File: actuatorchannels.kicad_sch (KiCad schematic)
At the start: 3 parts

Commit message: Array of SSRs for actuation channels
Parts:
- added D? (x16): B2100A-13-F, Diode_SMD:D_SMA, symbol Device:D_Schottky_Small_Filled
- added J? (x16): ACT CH1, TerminalBlock_Phoenix:TerminalBlock_Phoenix_PT-1,5-2-5.0-H_1x02_P5.00mm_Horizontal, symbol Connector:Screw_Terminal_01x02
- added R? (x15): 270R, Resistor_SMD:R_0603_1608Metric, symbol Device:R_Small_US
- added U? (x15): TLP241A, actuation:11-5B2S, symbol actuation:TLP241A
- R?: value R_Small_US -> 270R; footprint (none) -> Resistor_SMD:R_0603_1608Metric; MPN (none) -> RC0603FR-07270RL
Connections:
- net ACT_CH1: now also R?.1, R?.1, R?.1, R?.1, R?.1, R?.1, R?.1, R?.1, R?.1, R?.1, R?.1, R?.1, R?.1, R?.1, R?.1
- net GND: now also U?.2, U?.2, U?.2, U?.2, U?.2, U?.2, U?.2, U?.2, U?.2, U?.2, U?.2, U?.2, U?.2, U?.2, U?.2
- net at U?.3: now also D?.1 (K), J?.1 (Pin_1)
- net Vdrive: now reaches U?.4
- net Vdrive: now also U?.4, U?.4, U?.4, U?.4, U?.4, U?.4, U?.4, U?.4, U?.4, U?.4, U?.4, U?.4, U?.4, U?.4, U?.4
- new net: R?.2, U?.1 (x15)
- new net: D?.1 (K), J?.1 (Pin_1), U?.3 (x15)
- new net GNDPWR: D?.2 (A), D?.2 (A), D?.2 (A), D?.2 (A), D?.2 (A), D?.2 (A), D?.2 (A), D?.2 (A), D?.2 (A), D?.2 (A), D?.2 (A), D?.2 (A), D?.2 (A), D?.2 (A), D?.2 (A), D?.2 (A), J?.2 (Pin_2), J?.2 (Pin_2), J?.2 (Pin_2), J?.2 (Pin_2), J?.2 (Pin_2), J?.2 (Pin_2), J?.2 (Pin_2), J?.2 (Pin_2), J?.2 (Pin_2), J?.2 (Pin_2), J?.2 (Pin_2), J?.2 (Pin_2), J?.2 (Pin_2), J?.2 (Pin_2), J?.2 (Pin_2), J?.2 (Pin_2)
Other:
- moved on the sheet: R?, U?
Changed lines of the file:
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@@
 (kicad_sch (version 20211123) (generator eeschema)
-  (paper "A3")
+  (paper "A2")

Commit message: Actuator channels complete
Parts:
- added C? (x2): 1uF, Capacitor_SMD:C_0603_1608Metric, symbol Device:C_Small
- added C? (x2): 0.1uF, Capacitor_SMD:C_0603_1608Metric, symbol Device:C_Small
- added U?: PCA9534, Package_SO:TSSOP-16_4.4x5mm_P0.65mm, symbol actuation:PCA9534
- J?: value ACT CH1 -> ACT CH3
- J?: value ACT CH1 -> ACT CH14
- J?: value ACT CH1 -> ACT CH2
- J?: value ACT CH1 -> ACT CH8
- J?: value ACT CH1 -> ACT CH12
- J?: value ACT CH1 -> ACT CH13
- J?: value ACT CH1 -> ACT CH7
- J?: value ACT CH1 -> ACT CH11
- J?: value ACT CH1 -> ACT CH16
- J?: value ACT CH1 -> ACT CH4
- J?: value ACT CH1 -> ACT CH9
- J?: value ACT CH1 -> ACT CH10
- J?: value ACT CH1 -> ACT CH15
- J?: value ACT CH1 -> ACT CH6
- J?: value ACT CH1 -> ACT CH5
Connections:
- net ACT_CH1: now also U?.4 (P0); no longer R?.1, R?.1, R?.1, R?.1, R?.1, R?.1, R?.1, R?.1, R?.1, R?.1, R?.1, R?.1, R?.1, R?.1, R?.1
- net GND: now also U?.1 (A0), U?.2 (A1), U?.3 (A2), U?.8 (GND), C?.2, C?.2, C?.2, C?.2, U?.2 (A1), U?.3 (A2), U?.8 (GND)
- net ACT_CH6: now reaches U?.10 (P5)
- net ACT_CH6: now also R?.1
- net ACT_CH7: now reaches U?.11 (P6)
- net ACT_CH7: now also R?.1
- net ACT_CH8: now reaches U?.12 (P7)
- net ACT_CH8: now also R?.1
- net SCL: now reaches U?.14 (SCL)
- net SCL: now also U?.14 (SCL)
- net SDA: now reaches U?.15 (SDA)
- net SDA: now also U?.15 (SDA)
- net +3.3V: now reaches U?.16 (VCC)
- net +3.3V: now also C?.1, C?.1, C?.1, C?.1, U?.1 (A0), U?.16 (VCC)
- net ACT_CH2: now reaches U?.5 (P1)
- net ACT_CH2: now also R?.1
- net ACT_CH3: now reaches U?.6 (P2)
- net ACT_CH3: now also R?.1
- net ACT_CH4: now reaches U?.7 (P3)
- net ACT_CH4: now also R?.1
- net ACT_CH5: now reaches U?.9 (P4)
- net ACT_CH5: now also R?.1
- new net ACT_CH10: R?.1, U?.5 (P1)
- new net ACT_CH11: R?.1, U?.6 (P2)
- new net ACT_CH12: R?.1, U?.7 (P3)
- new net ACT_CH13: R?.1, U?.9 (P4)
- new net ACT_CH14: R?.1, U?.10 (P5)
- new net ACT_CH15: R?.1, U?.11 (P6)
- new net ACT_CH16: R?.1, U?.12 (P7)
- new net ACT_CH9: R?.1, U?.4 (P0)
- no-connect marks 0 -> 2
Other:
- moved on the sheet: D?, J?, R?, U?
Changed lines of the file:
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@@
 (kicad_sch (version 20211123) (generator eeschema)
-  (paper "A2")
+  (paper "User" 299.999 350.012)

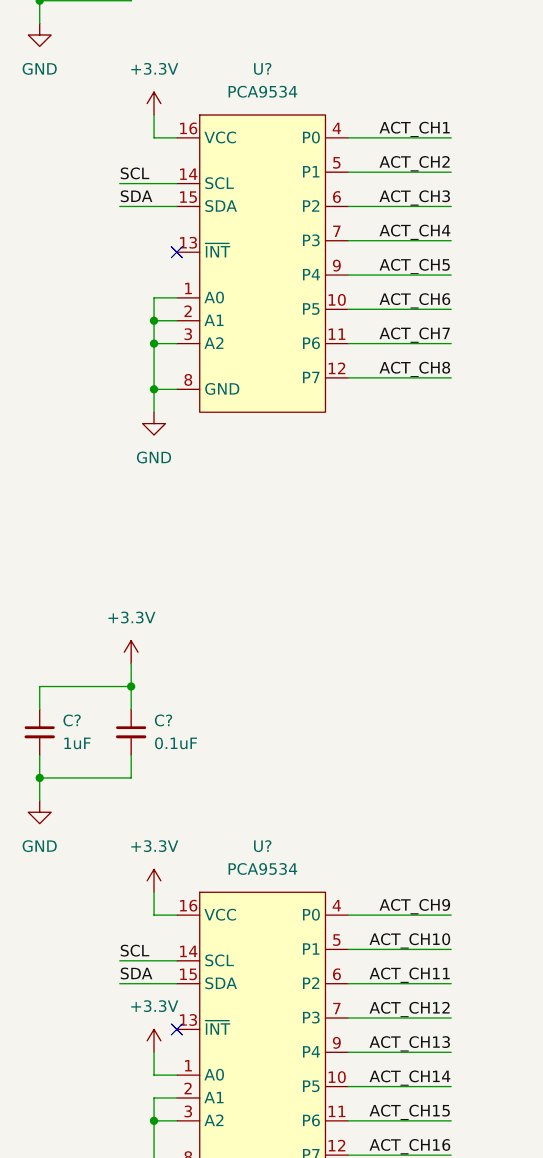
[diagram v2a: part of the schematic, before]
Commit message: Array of isolators for feedback channels
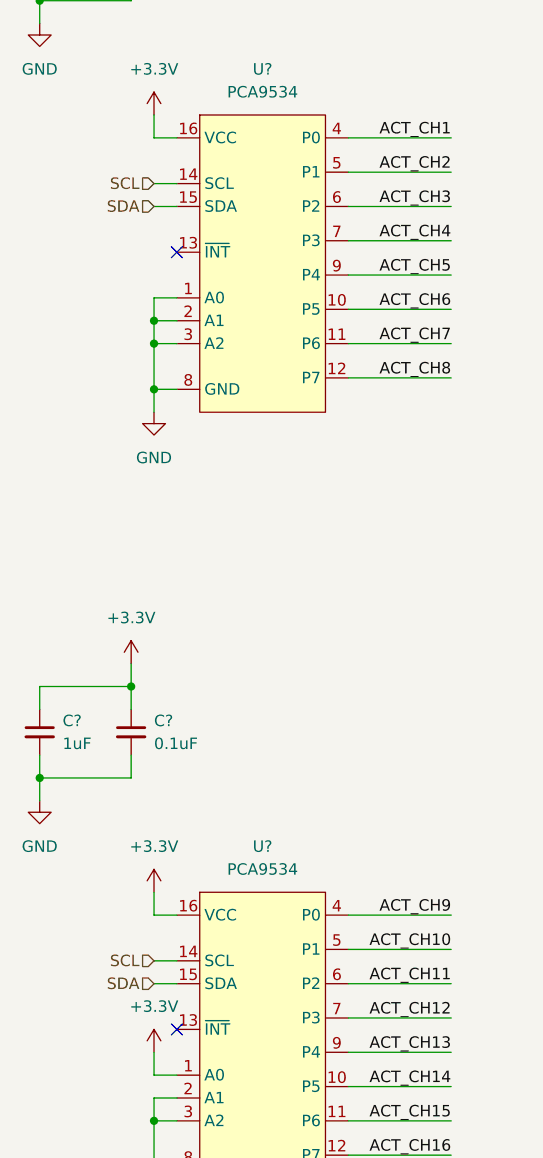
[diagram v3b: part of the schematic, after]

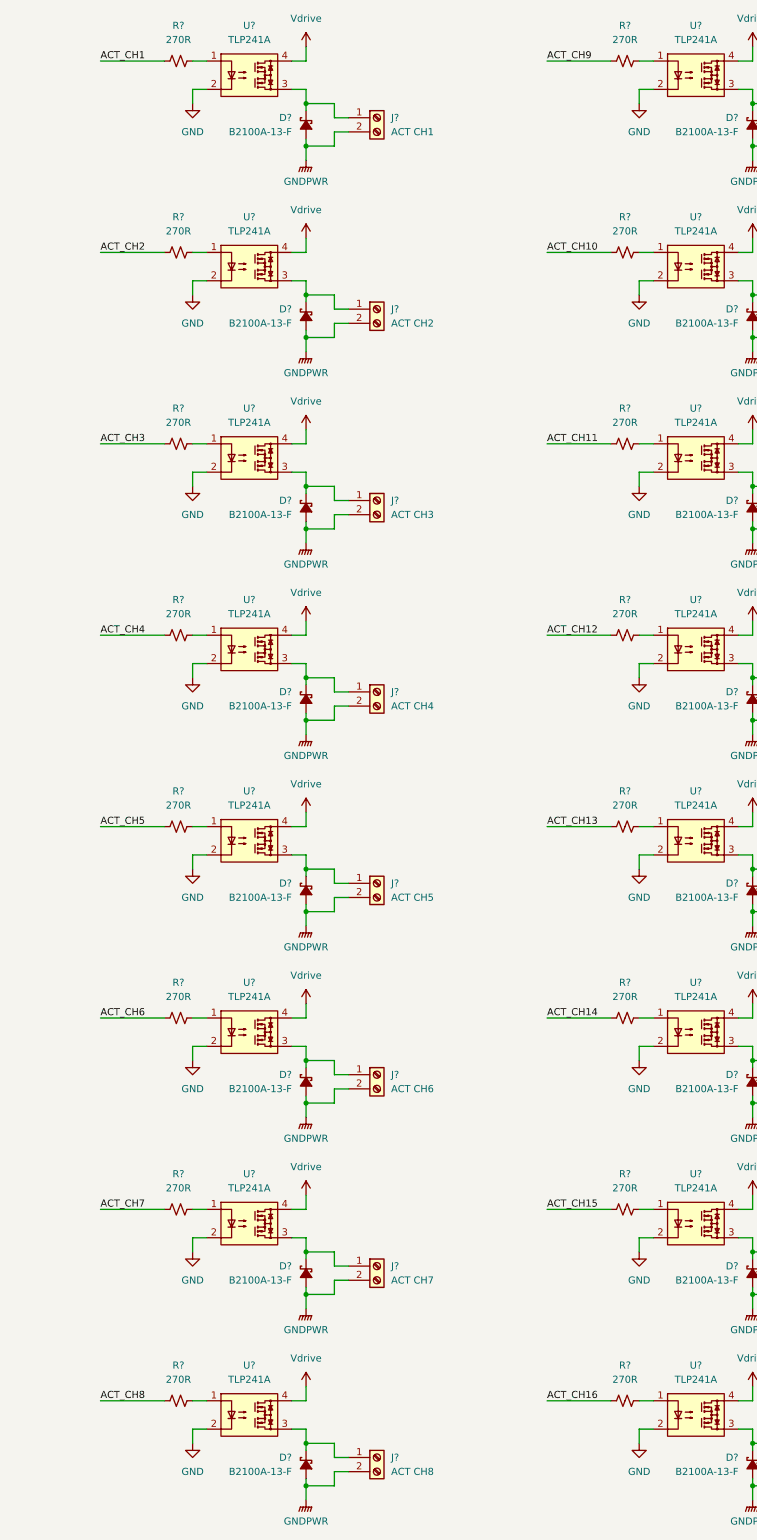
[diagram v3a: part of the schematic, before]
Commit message: Fixed actuator channels to make GPIO expander sink instead of source current
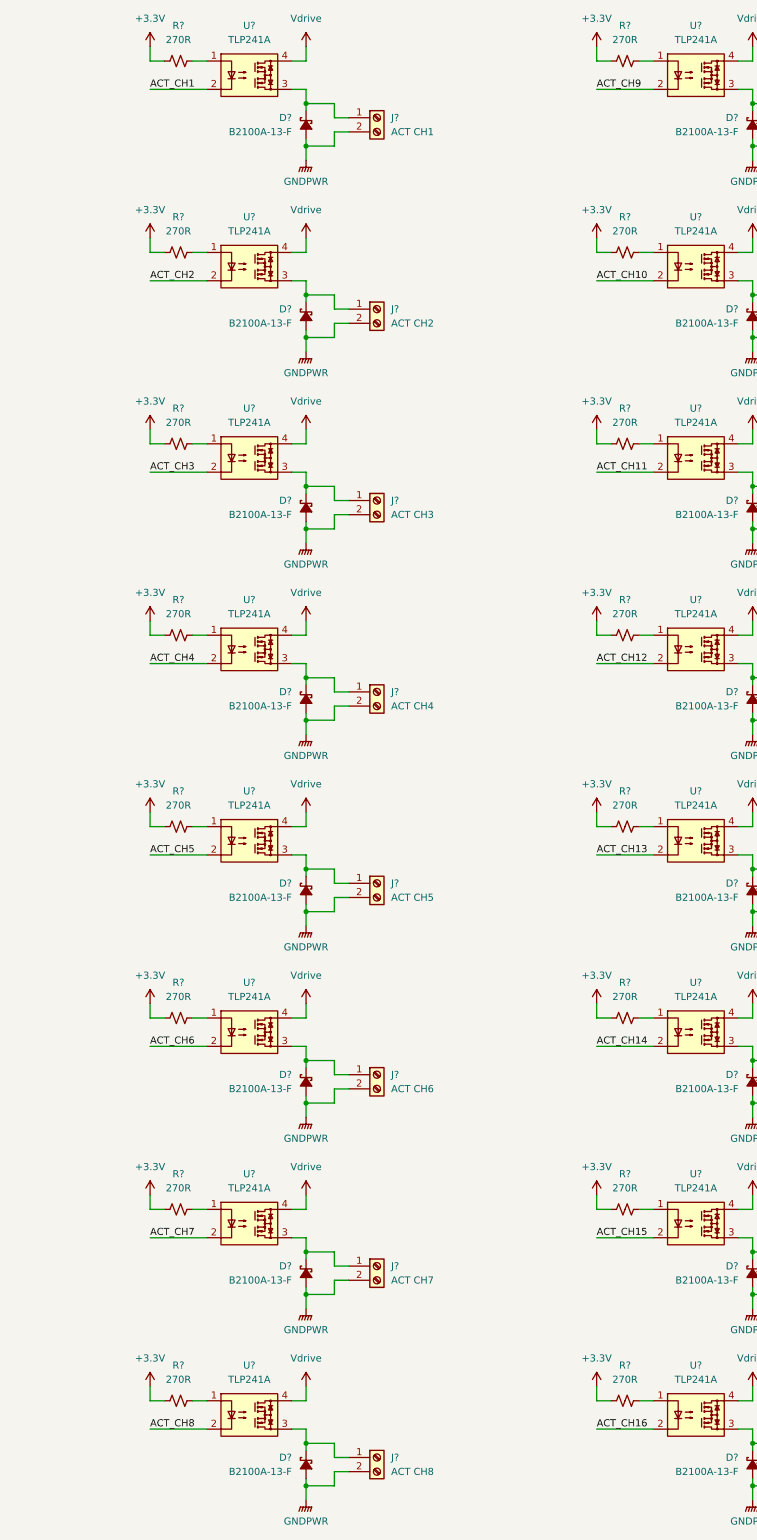
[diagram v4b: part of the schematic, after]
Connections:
- net +3.3V: now also R?.1, R?.1, R?.1, R?.1, R?.1, R?.1, R?.1, R?.1, R?.1, R?.1, R?.1, R?.1, R?.1, R?.1, R?.1, R?.1
- net ACT_CH1: now also U?.2; no longer R?.1
- net ACT_CH10: now also U?.2; no longer R?.1
- net ACT_CH11: now also U?.2; no longer R?.1
- net ACT_CH12: now also U?.2; no longer R?.1
- net ACT_CH13: now also U?.2; no longer R?.1
- net ACT_CH14: now also U?.2; no longer R?.1
- net ACT_CH15: now also U?.2; no longer R?.1
- net ACT_CH16: now also U?.2; no longer R?.1
- net ACT_CH2: now also U?.2; no longer R?.1
- net ACT_CH3: now also U?.2; no longer R?.1
- net ACT_CH4: now also U?.2; no longer R?.1
- net ACT_CH5: now also U?.2; no longer R?.1
- net ACT_CH6: now also U?.2; no longer R?.1
- net ACT_CH7: now also U?.2; no longer R?.1
- net ACT_CH8: now also U?.2; no longer R?.1
- net ACT_CH9: now also U?.2; no longer R?.1
- net GND: no longer U?.2, U?.2, U?.2, U?.2, U?.2, U?.2, U?.2, U?.2, U?.2, U?.2, U?.2, U?.2, U?.2, U?.2, U?.2, U?.2

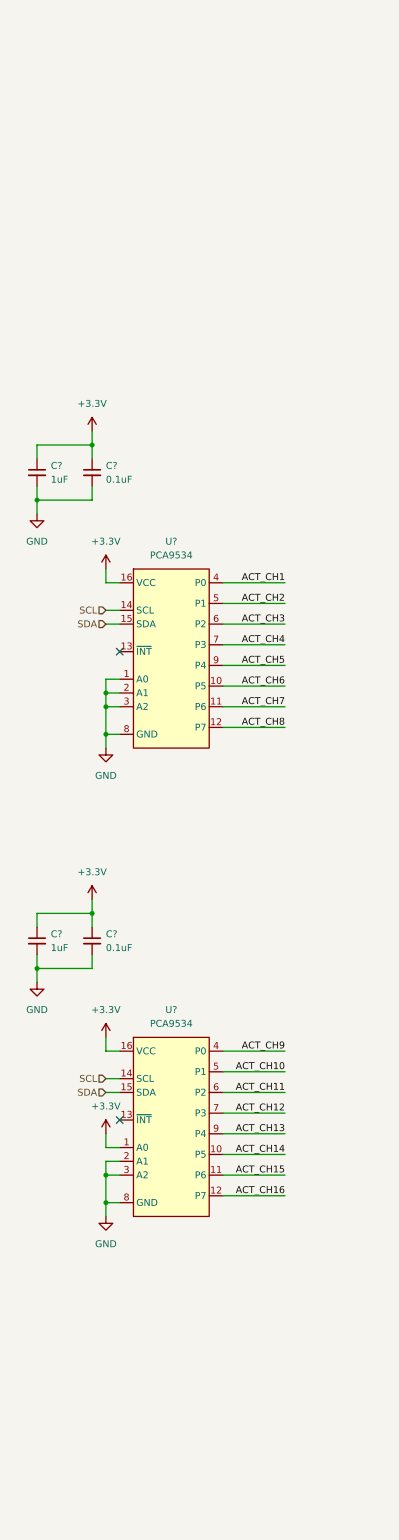
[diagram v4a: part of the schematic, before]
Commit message: Added actuation status LEDs
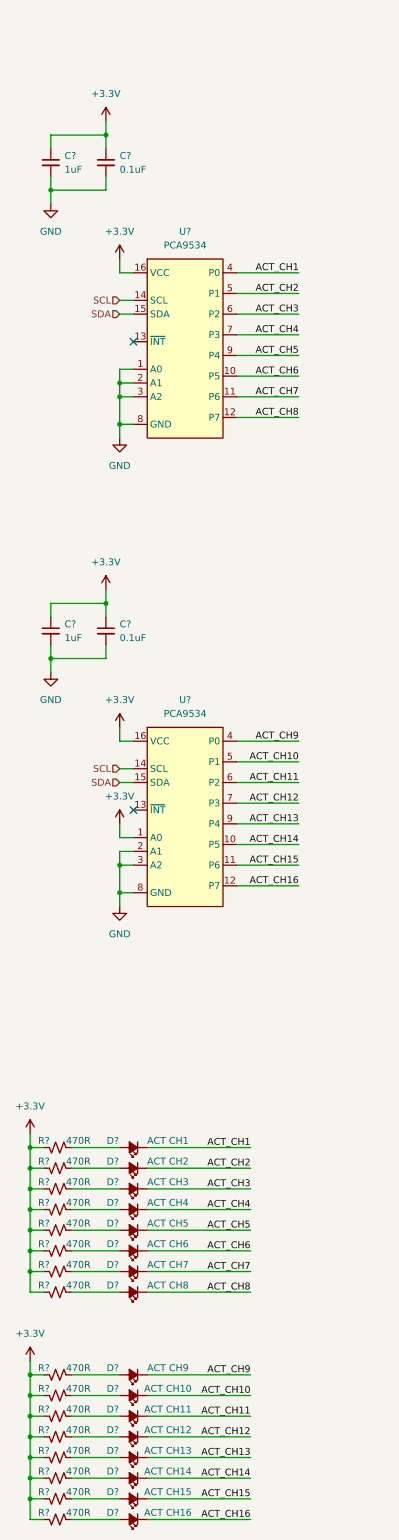
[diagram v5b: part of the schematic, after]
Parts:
- added D?: ACT CH13, symbol Device:LED_Small_Filled
- added D?: ACT CH14, symbol Device:LED_Small_Filled
- added D?: ACT CH7, symbol Device:LED_Small_Filled
- added D?: ACT CH8, symbol Device:LED_Small_Filled
- added D?: ACT CH16, symbol Device:LED_Small_Filled
- added D?: ACT CH1, symbol Device:LED_Small_Filled
- added D?: ACT CH12, symbol Device:LED_Small_Filled
- added D?: ACT CH5, symbol Device:LED_Small_Filled
- added D?: ACT CH15, symbol Device:LED_Small_Filled
- added D?: ACT CH3, symbol Device:LED_Small_Filled
- added D?: ACT CH4, symbol Device:LED_Small_Filled
- added D?: ACT CH10, symbol Device:LED_Small_Filled
- added D?: ACT CH9, symbol Device:LED_Small_Filled
- added D?: ACT CH11, symbol Device:LED_Small_Filled
- added D?: ACT CH6, symbol Device:LED_Small_Filled
- added D?: ACT CH2, symbol Device:LED_Small_Filled
- added R? (x16): 470R, symbol Device:R_Small_US
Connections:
- net +3.3V: now also R?.1, R?.1, R?.1, R?.1, R?.1, R?.1, R?.1, R?.1, R?.1, R?.1, R?.1, R?.1, R?.1, R?.1, R?.1, R?.1
- net ACT_CH1: now also D?.1 (K)
- net ACT_CH10: now also D?.1 (K)
- net ACT_CH11: now also D?.1 (K)
- net ACT_CH12: now also D?.1 (K)
- net ACT_CH13: now also D?.1 (K)
- net ACT_CH14: now also D?.1 (K)
- net ACT_CH15: now also D?.1 (K)
- net ACT_CH16: now also D?.1 (K)
- net ACT_CH2: now also D?.1 (K)
- net ACT_CH3: now also D?.1 (K)
- net ACT_CH4: now also D?.1 (K)
- net ACT_CH5: now also D?.1 (K)
- net ACT_CH6: now also D?.1 (K)
- net ACT_CH7: now also D?.1 (K)
- net ACT_CH8: now also D?.1 (K)
- net ACT_CH9: now also D?.1 (K)
- new net: D?.2 (A), R?.2 (x16)
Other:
- moved on the sheet: C?, U?

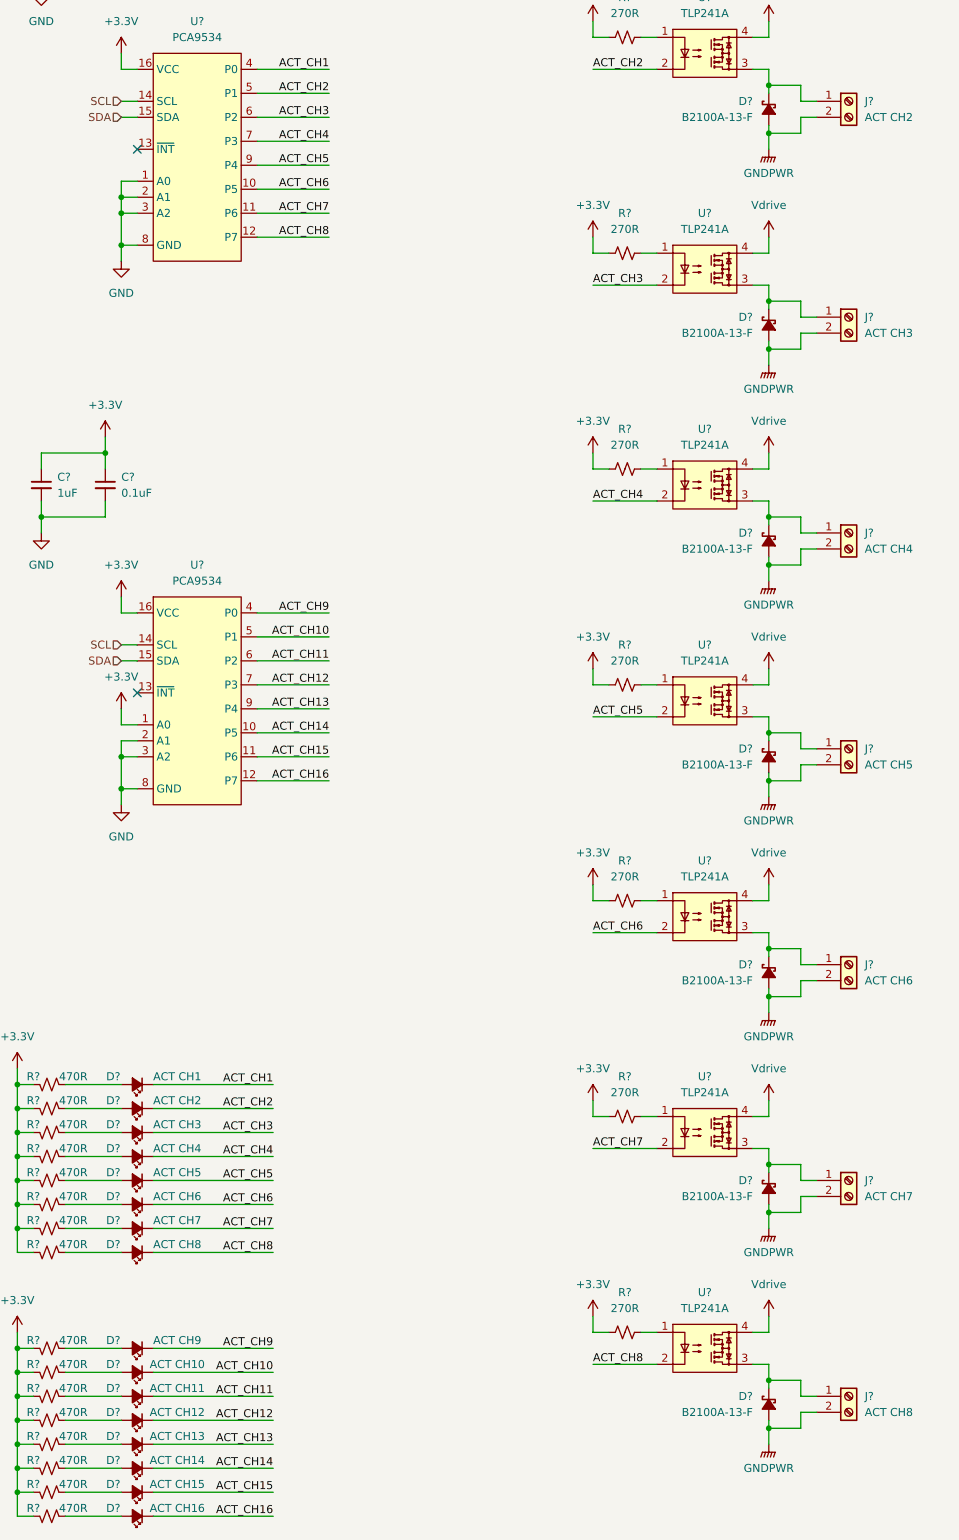
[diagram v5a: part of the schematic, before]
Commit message: Created arming circuit controllable by C&C
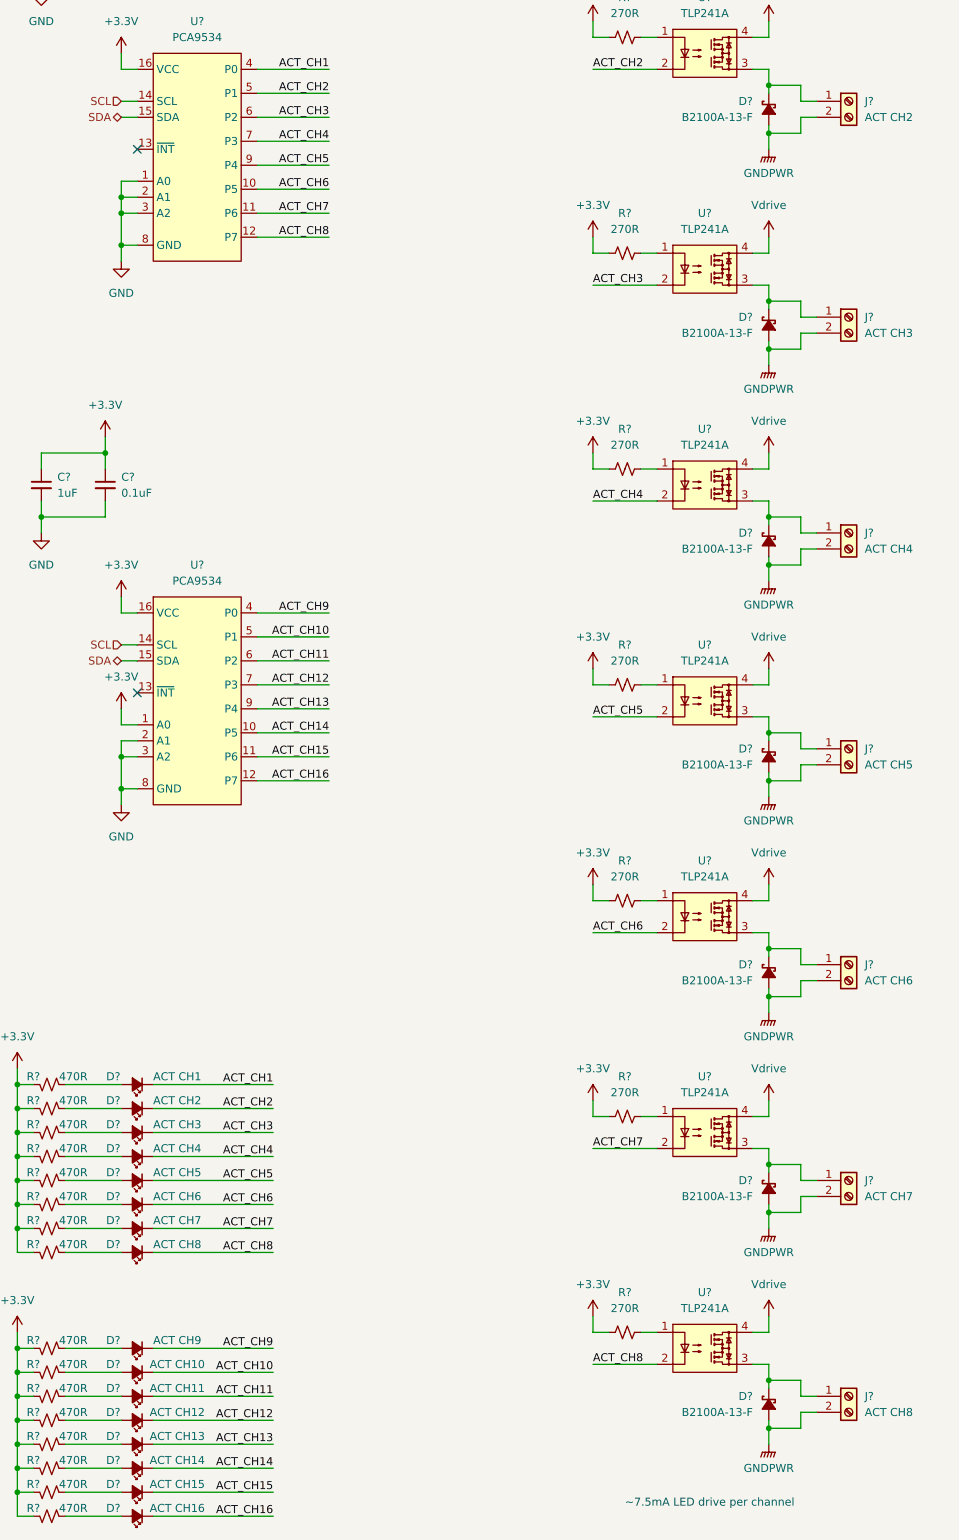
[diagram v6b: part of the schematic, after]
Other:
- note added: "~7.5mA LED drive per channel"

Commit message: Reorganizing schematic
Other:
- note added: "Actuation Logic (COLD)"
- note added: "Actuation Logic (HOT)"
- moved on the sheet: C?, D?, J?, R?, U?
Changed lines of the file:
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@@
 (kicad_sch (version 20211123) (generator eeschema)
-  (paper "User" 299.999 350.012)
+  (paper "User" 299.999 340.004)

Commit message: More reorganizing
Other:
- note added: "Actuation Logic"
- note added: "Actuation SSRs"
- note removed: "Actuation Logic (COLD)"
- note removed: "Actuation Logic (HOT)"
